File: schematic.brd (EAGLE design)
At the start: 100 x 80 mm, 32 parts, among them Q3 IRF540, Q5 SPB80P06P

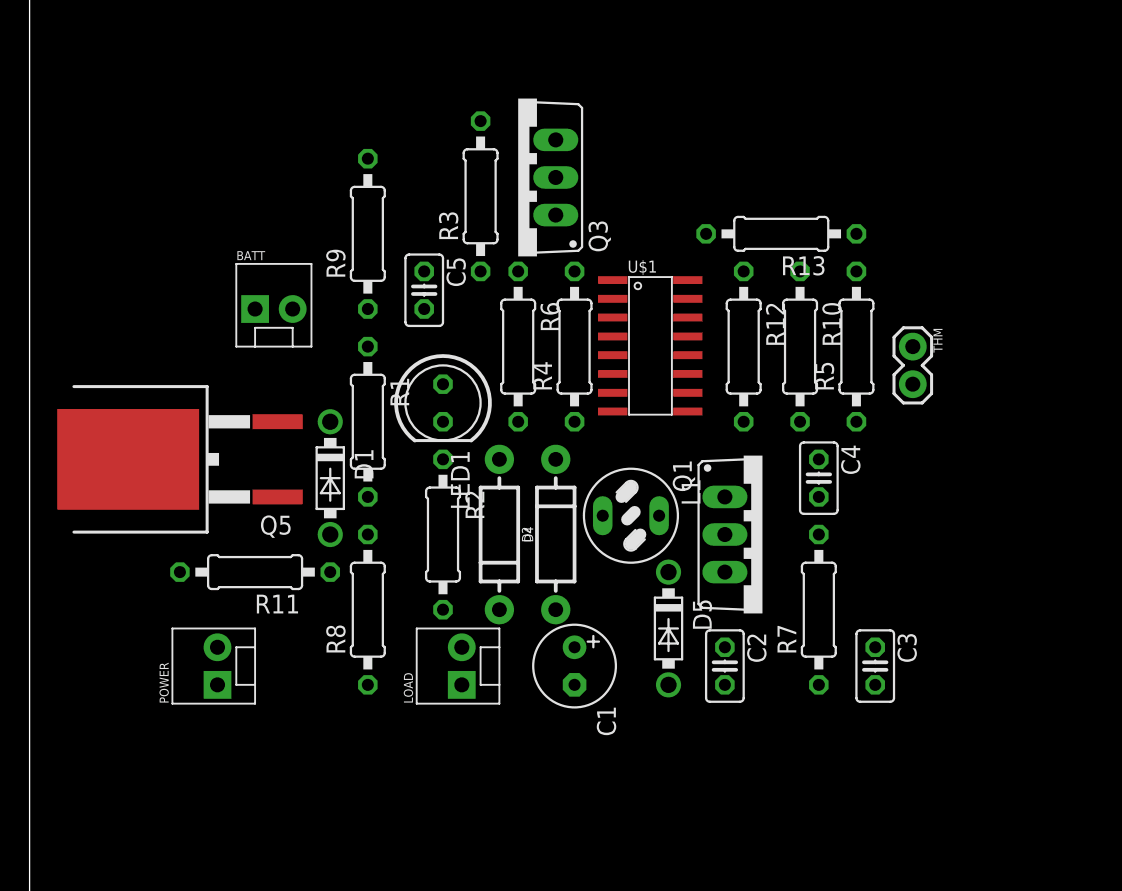
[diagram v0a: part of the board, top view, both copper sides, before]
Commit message: start drawing the board
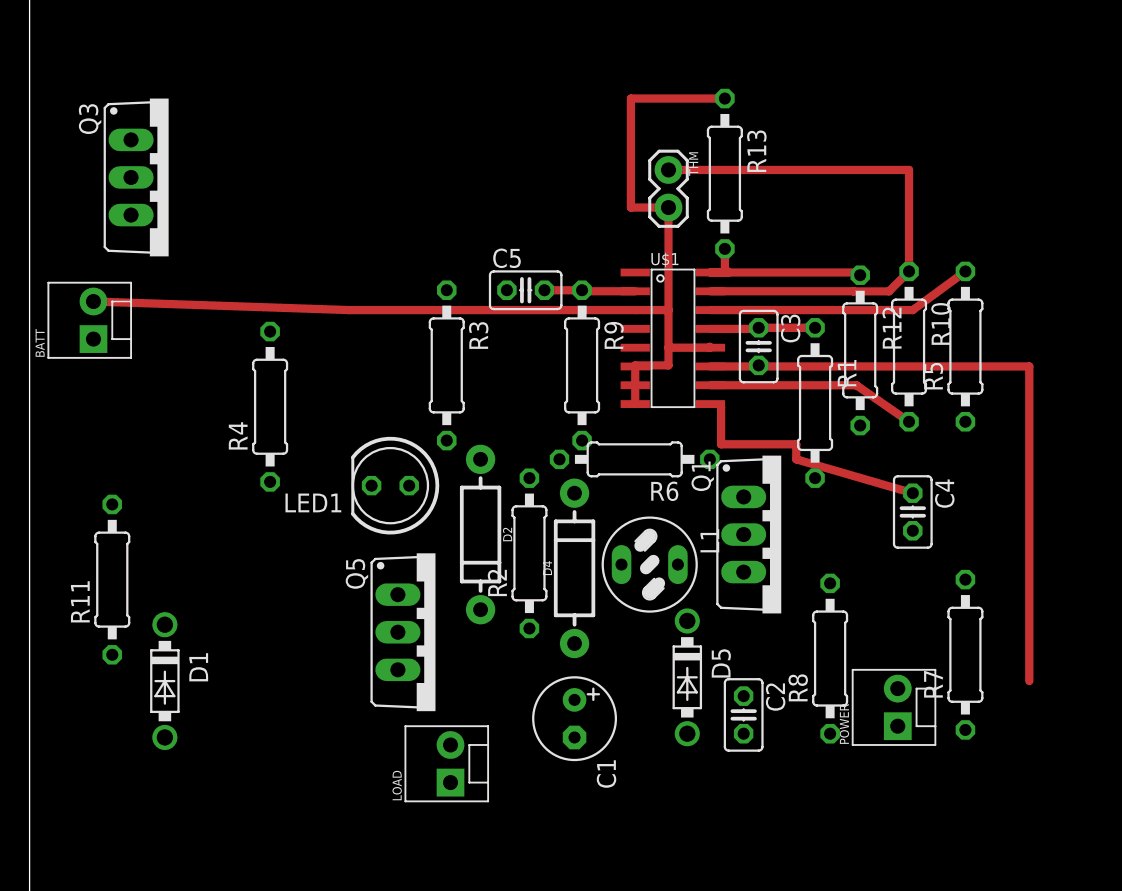
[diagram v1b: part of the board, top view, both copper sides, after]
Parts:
- Q5: value SPB80P06P -> (none); device transistor-fet:TO263 -> transistor-power:TO220BV
- moved POWER 46.1 mm to (58.7, 21.3)
- moved R8 31.4 mm to (54.1, 25.9)
- moved R1 30.3 mm to (53.1, 43.2)
- moved Q3 23.6 mm to (9.40, 58.4), turned to 270 degrees
- moved C3 23.0 mm to (49.3, 47.0)
- moved R4 21.0 mm to (16.3, 42.9)
- moved Q5 20.9 mm to (27.4, 27.7), turned to 270 degrees
- moved THM 20.4 mm to (43.2, 58.9)
- moved D1 17.7 mm to (9.14, 24.4)
- moved R9 17.0 mm to (37.3, 45.7), turned to 270 degrees
- moved R3 11.7 mm to (28.2, 45.7), turned to 270 degrees
- moved BATT 11.1 mm to (4.32, 47.5), turned to 90 degrees
- moved R6 11.0 mm to (40.9, 39.4), turned to 180 degrees
- moved R7 10.4 mm to (63.2, 26.2)
- moved R11 9.67 mm to (5.59, 31.2), turned to 90 degrees
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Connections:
- net N$1: now also Q5.G; no longer Q5.1
- net N$26: now also Q5.S; no longer Q5.2
- net N$8: now also Q5.D; no longer Q5.3
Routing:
- net N$4: track 0.00 -> 73.6 mm
- net GND: track 0.00 -> 43.1 mm
- net N$5: track 0.00 -> 37.1 mm
- net N$20: track 0.00 -> 18.1 mm
- net N$23: track 0.00 -> 16.8 mm
- net N$7: track 0.00 -> 14.5 mm
- net N$6: track 0.00 -> 14.2 mm
- net N$19: track 0.00 -> 7.14 mm
- net N$12: track 0.00 -> 6.21 mm

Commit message: Layout done
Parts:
- C5: value (none) -> 1nF
- R12: value 200k -> 500k
- R5: value 47k -> 160k
- R8: value (none) -> 100k
- moved BATT 36.9 mm to (38.6, 33.8)
- moved R11 22.9 mm to (27.9, 36.1), turned to 180 degrees
- moved R6 18.9 mm to (30.5, 23.6), turned to 270 degrees
- moved R7 18.3 mm to (53.8, 41.9)
- moved Q3 17.7 mm to (23.9, 48.3)
- moved D1 15.1 mm to (24.1, 22.4), turned to 90 degrees
- moved R4 14.8 mm to (31.0, 43.7)
- moved LOAD 14.5 mm to (42.9, 17.3), turned to 180 degrees
- moved Q5 8.82 mm to (21.6, 21.1)
- moved R13 8.52 mm to (54.6, 54.9), turned to 0 degrees
- moved D4 8.39 mm to (37.1, 23.6), turned to 270 degrees
- moved D2 7.44 mm to (23.1, 33.3), turned to 0 degrees
- moved POWER 6.35 mm to (62.5, 26.4)
- moved Q1 5.86 mm to (52.6, 28.7)
- moved LED1 5.14 mm to (19.3, 38.4), turned to 90 degrees
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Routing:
- net GND: track 43.1 -> 171.8 mm, vias 0 -> 2
- net N$26: track 0.00 -> 116.5 mm
- net N$8: track 0.00 -> 96.3 mm
- net N$25: track 0.00 -> 73.3 mm, vias 0 -> 2
- net N$13: track 0.00 -> 59.2 mm, vias 0 -> 2
- net N$23: track 16.8 -> 45.3 mm, vias 0 -> 4
- net N$14: track 0.00 -> 16.3 mm
- net N$1: track 0.00 -> 16.3 mm
- net N$15: track 0.00 -> 12.7 mm, vias 0 -> 2
- net N$12: track 6.21 -> 18.6 mm
- net N$10: track 0.00 -> 11.6 mm
- net N$9: track 0.00 -> 10.5 mm
- net N$4: track 73.6 -> 82.9 mm
- net N$5: track 37.1 -> 45.5 mm
- net N$6: track 14.2 -> 19.7 mm
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
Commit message: Create pdf with pcb
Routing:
- net GND: track 171.8 -> 172.8 mm
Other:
- board size 100 x 80 mm -> 57.1 x 54.6 mm
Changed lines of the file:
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@@
 <setting verticaltext="up"/>
 </settings>
-<grid distance="10" unitdist="mil" unit="mil" style="lines" multiple="1" display="yes" altdistance="5" altunitdist="mil" altunit="mil"/>
+<grid distance="10" unitdist="mil" unit="mil" style="lines" multiple="1" display="no" altdistance="5" altunitdist="mil" altunit="mil"/>
 <layers>
 <layer number="1" name="Top" color="4" fill="1" visible="yes" active="yes"/>
@@
 <layer number="47" name="Measures" color="7" fill="1" visible="no" active="yes"/>
 <layer number="48" name="Document" color="7" fill="1" visible="yes" active="yes"/>
-<layer number="49" name="Reference" color="7" fill="1" visible="yes" active="yes"/>
+<layer number="49" name="Reference" color="7" fill="1" visible="no" active="yes"/>
 <layer number="50" name="dxf" color="7" fill="1" visible="no" active="no"/>
 <layer number="51" name="tDocu" color="7" fill="1" visible="yes" active="yes"/>
@@
 <board>
 <plain>
-<wire x1="0" y1="0" x2="100" y2="0" width="0" layer="20"/>
-<wire x1="100" y1="0" x2="100" y2="80" width="0" layer="20"/>
-<wire x1="100" y1="80" x2="0" y2="80" width="0" layer="20"/>
-<wire x1="0" y1="80" x2="0" y2="0" width="0" layer="20"/>
+<wire x1="12.7" y1="8.89" x2="69.774" y2="8.89" width="0" layer="20"/>
+<wire x1="69.774" y1="8.89" x2="69.774" y2="63.49" width="0" layer="20"/>
+<wire x1="69.774" y1="63.49" x2="12.7" y2="63.49" width="0" layer="20"/>
+<wire x1="12.7" y1="63.49" x2="12.7" y2="8.89" width="0" layer="20"/>
 </plain>
 <attributes>
@@
 <wire x1="51.236" y1="45.648" x2="46.014" y2="45.648" width="0.5588" layer="1"/>
 <wire x1="51.308" y1="45.72" x2="51.236" y2="45.648" width="0.5588" layer="1"/>
-<wire x1="51.308" y1="45.72" x2="51.562" y2="45.72" width="0.5588" layer="1"/>
 <via x="51.562" y="45.72" extent="1-16" drill="0.9"/>
 <via x="51.562" y="38.354" extent="1-16" drill="0.9"/>
@@
 <wire x1="43.688" y1="21.844" x2="46.228" y2="19.304" width="1.524" layer="1"/>
 <wire x1="50.038" y1="17.78" x2="53.848" y2="17.78" width="1.778" layer="1"/>
+<wire x1="51.562" y1="45.72" x2="52.07" y2="45.72" width="0.6604" layer="1"/>
+<wire x1="52.07" y1="45.72" x2="51.308" y2="45.72" width="0.6604" layer="1"/>
 </signal>
 <signal name="N$4">

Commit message: Add new board
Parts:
- Q1: value (none) -> FDN360P; device transistor-power:TO220BV -> transistor-power:SUPER-SOT3
- Q3: value IRF540 -> BSS123; device transistor-power:TO220BV -> transistor-small-signal:SOT23
- moved R12 104.2 mm to (-44.5, 50.8), turned to 0 degrees
- moved D5 98.6 mm to (-52.1, 15.2), turned to 0 degrees
- moved C4 98.2 mm to (-34.3, 22.9)
- moved R5 98.0 mm to (-31.8, 40.6), turned to 0 degrees
- moved POWER 93.6 mm to (-30.5, 15.2), turned to 0 degrees
- moved C2 90.8 mm to (-40.6, 22.9), turned to 0 degrees
- moved R8 90.5 mm to (-31.8, 45.7), turned to 0 degrees
- moved C5 82.6 mm to (-47.0, 22.9)
- moved R10 82.1 mm to (-19.1, 50.8), turned to 0 degrees
- moved C3 80.9 mm to (-27.9, 22.9), turned to 0 degrees
- moved D4 80.5 mm to (-43.2, 29.2), turned to 0 degrees
- moved R9 78.7 mm to (-44.5, 45.7), turned to 0 degrees
- moved R6 76.8 mm to (-44.5, 40.6), turned to 0 degrees
- moved R1 76.3 mm to (-19.1, 35.6), turned to 0 degrees
- moved R13 73.7 mm to (-19.1, 55.9)
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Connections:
- net N$10: now also Q1.3; no longer Q1.D
- net N$13: now also Q1.1, Q3.2; no longer Q1.G, Q3.S
- net N$14: now also Q3.1; no longer Q3.G
- net N$26: now also Q1.2, Q3.3; no longer Q1.S, Q3.D
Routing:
- net GND: track 172.8 -> 0.00 mm, vias 2 -> 0
- net N$26: track 116.5 -> 0.00 mm
- net N$8: track 96.3 -> 0.00 mm
- net N$4: track 82.9 -> 0.00 mm
- net N$25: track 73.3 -> 0.00 mm, vias 2 -> 0
- net N$13: track 59.2 -> 0.00 mm, vias 2 -> 0
- net N$5: track 45.5 -> 0.00 mm
- net N$23: track 45.3 -> 0.00 mm, vias 4 -> 0
- net N$20: track 22.4 -> 0.00 mm
- net N$6: track 19.7 -> 0.00 mm
- net N$7: track 19.4 -> 0.00 mm
- net N$12: track 18.6 -> 0.00 mm
- net N$14: track 16.3 -> 0.00 mm
- net N$1: track 16.3 -> 0.00 mm
- net N$15: track 12.7 -> 0.00 mm, vias 2 -> 0
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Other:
- board size 57.1 x 54.6 mm -> 100 x 80 mm
